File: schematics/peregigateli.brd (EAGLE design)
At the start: 100 x 80 mm, 18 parts

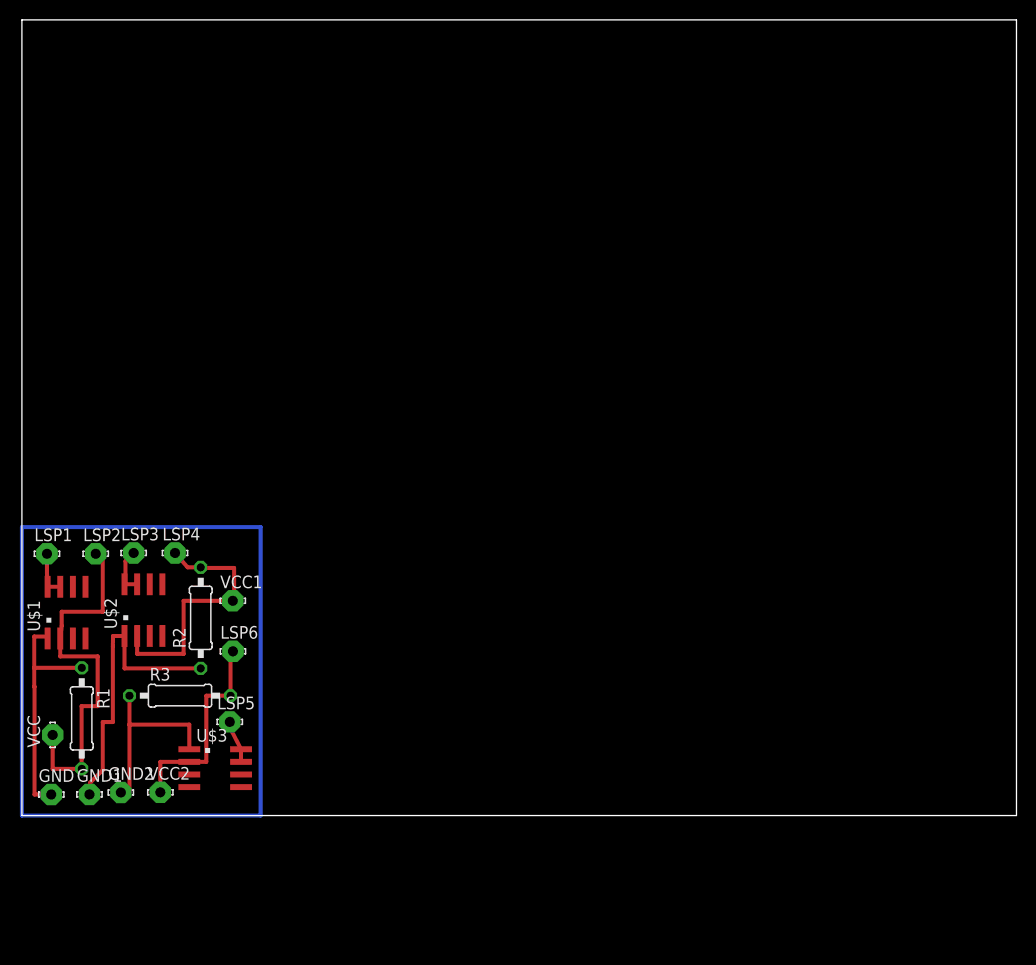
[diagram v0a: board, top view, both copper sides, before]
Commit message: плата с пережигателями
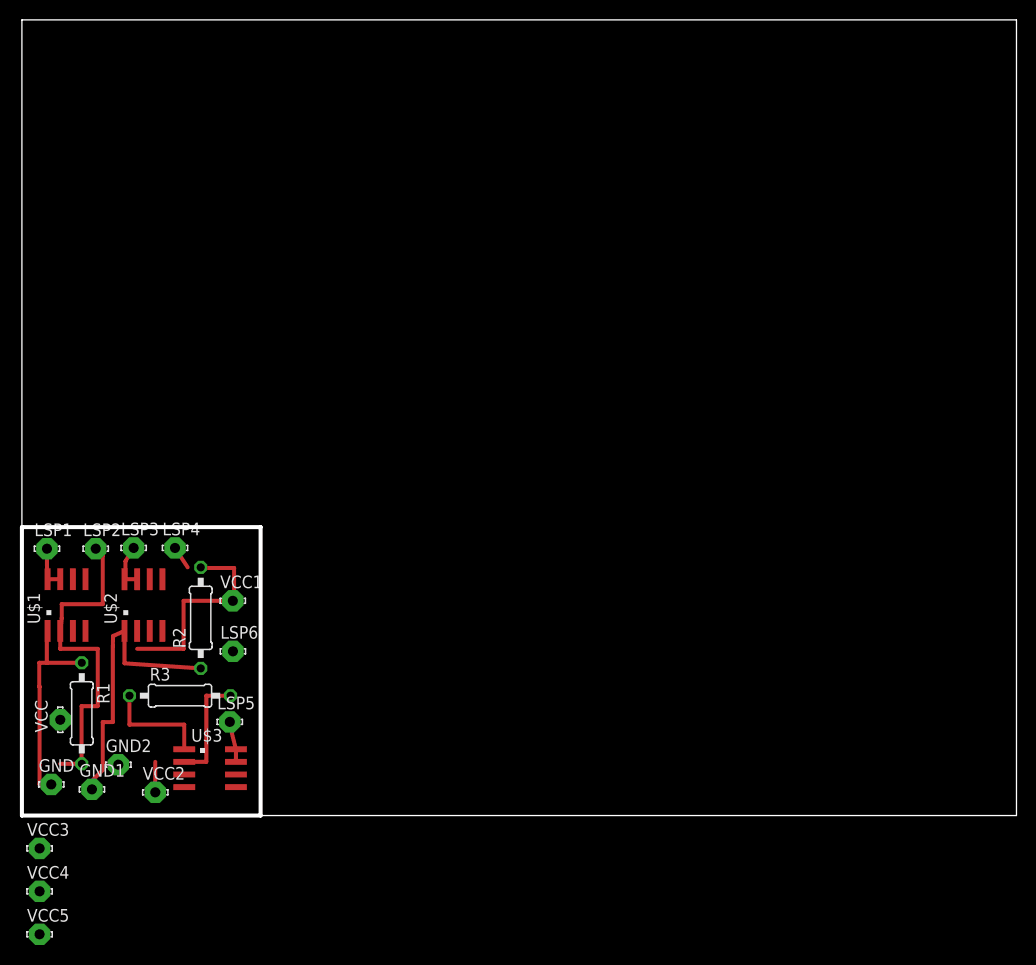
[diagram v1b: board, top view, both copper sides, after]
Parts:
- added VCC3, VCC4, VCC5: LSP10, solpad:LSP10
- moved GND2 2.81 mm to (9.69, 5.11)
- moved VCC 1.70 mm to (3.85, 9.63)
- moved GND 1.02 mm to (2.95, 3.13)
- moved U$1 0.76 mm to (4.49, 21.2)
- moved GND1 0.57 mm to (7.04, 2.63)
- moved LSP3 0.51 mm to (11.2, 26.9)
- moved LSP4 0.51 mm to (15.4, 26.9)
- moved LSP1 0.51 mm to (2.52, 26.8)
- moved LSP2 0.51 mm to (7.42, 26.8)
- moved R1 0.51 mm to (6.02, 10.3)
- moved U$2 0.51 mm to (12.2, 21.2)
- moved U$3 0.51 mm to (18.9, 4.76)
- moved VCC2 0.51 mm to (13.4, 2.34)
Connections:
- new net N$10: LSP2.MP, VCC.MP
- new net N$11: R2.2, U$2.2, VCC4.MP
- new net N$12: R3.2, U$3.2, VCC5.MP
- net N$2: now also VCC3.MP; no longer LSP2.MP, VCC.MP
- net N$5: no longer R2.2, U$2.2
- net N$8: no longer R3.2, U$3.2
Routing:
- net N$10: track 106.0 -> 0.00 mm
- net N$8: track 21.5 -> 3.31 mm
- net N$12: track 0.00 -> 11.3 mm
- net N$9: track 19.1 -> 10.9 mm
- net N$2: track 38.2 -> 33.4 mm
- net N$5: track 26.8 -> 23.6 mm
- net N$3: track 23.9 -> 21.4 mm
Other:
- outline, holes or cut-outs redrawn
